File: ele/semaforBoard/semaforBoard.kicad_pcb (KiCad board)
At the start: 2 copper layers, 52.1 x 21.6 mm, 25 parts, among them J1 RESET, J2 Flash_connector, J3 USB_A, Q1 BC817, Q2 BC817, Q3 BC817, SW1 SW_Push, U1 ESP-01, U2 AMS1117-3.3

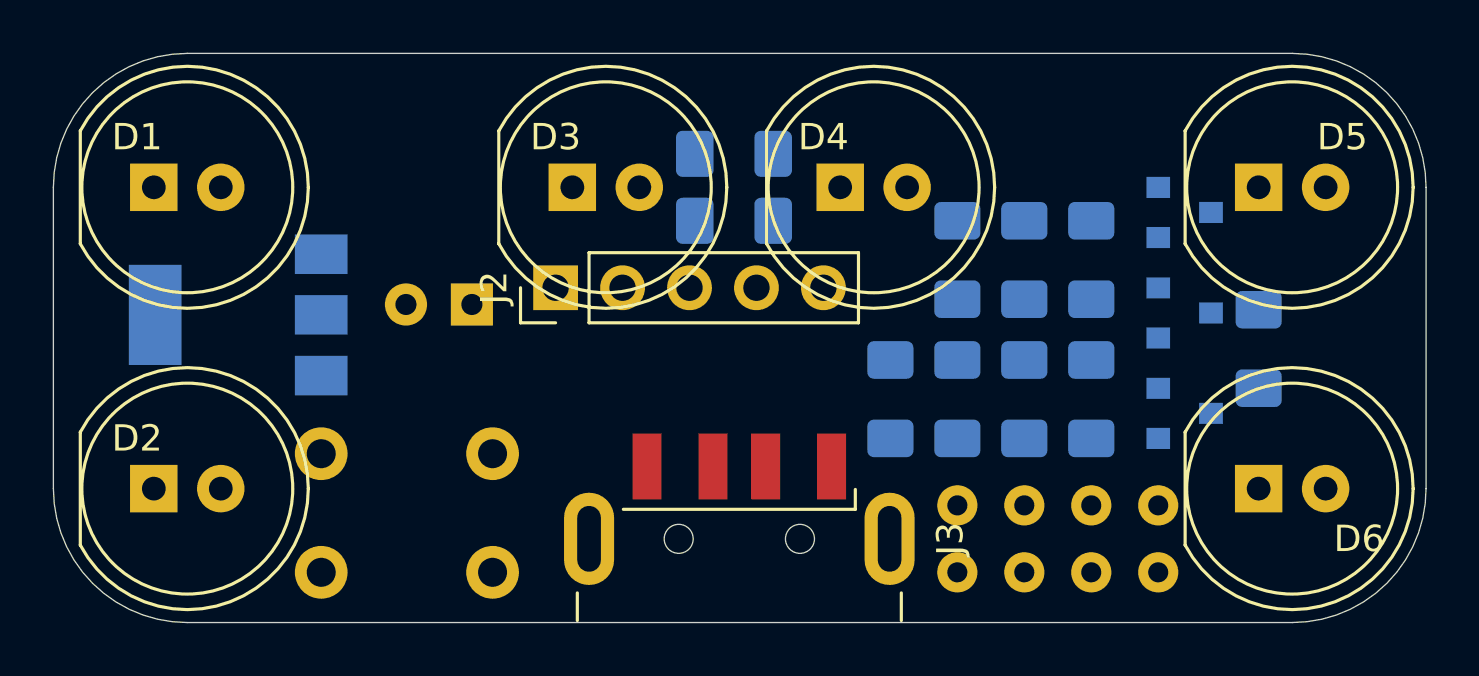
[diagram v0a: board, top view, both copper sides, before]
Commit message: Component placement, logos.
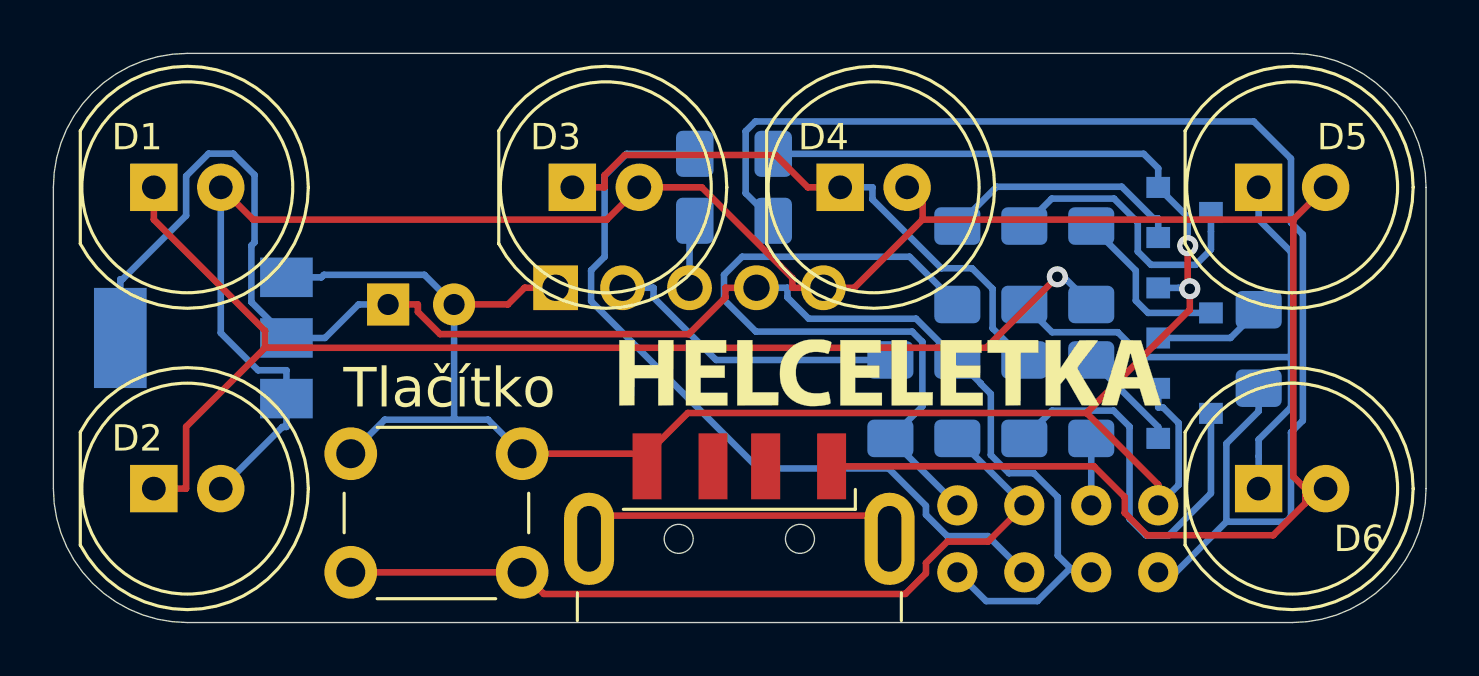
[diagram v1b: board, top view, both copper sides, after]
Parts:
- added G***: LOGO, semaforBoard:Robotarna, F.Cu at (154.4, 82.0)
- added G1: LOGO, semaforBoard:Robotarna, B.Cu at (129.0, 84.6)
- added G2: LOGO, semaforBoard:Helceletka, F.Cu at (148.6, 94.6)
- J2: moved to B.Cu
- SW1: moved to F.Cu
- moved SW1 4.64 mm to (134.6, 102.2)
- moved C1 3.18 mm to (129.5, 92.1), turned to 0 degrees
- moved U2 1.58 mm to (122.5, 93.3)
- moved R3 0.20 mm to (151.1, 90.6)
- moved R5 0.20 mm to (156.2, 90.6)
- moved R7 0.20 mm to (153.7, 90.6)
- turned J2 to 270 degrees
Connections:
- J2 pad 4: Net-(J2-Pad4) -> +3V3
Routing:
- net +5V: track 0.00 -> 93.6 mm
- net GND: track 0.00 -> 82.7 mm, vias 0 -> 2
- net +3V3: track 0.00 -> 62.7 mm
- net LED-A: track 0.00 -> 50.7 mm
- net Net-(D1-Pad1): track 0.00 -> 48.5 mm, vias 0 -> 1
- net BUTTON: track 0.00 -> 31.1 mm
- net RESET: track 0.00 -> 29.6 mm
- net LED-C: track 0.00 -> 26.8 mm
- net Net-(D5-Pad1): track 0.00 -> 23.4 mm
- net Net-(D3-Pad1): track 0.00 -> 22.3 mm
- net Net-(Q2-Pad3): track 0.00 -> 15.2 mm
- net Net-(J3-Pad5): track 0.00 -> 12.1 mm
- net Net-(J2-Pad2): track 0.00 -> 11.5 mm
- net Net-(Q3-Pad3): track 0.00 -> 10.8 mm
- net Net-(Q3-Pad1): track 0.00 -> 9.46 mm
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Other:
- board text added: "5V 3V3 TX RX GND"
- board text added: "Boot"
- board text added: "Semafor v0.1 05/20"
- board text added: "Tlačítko"

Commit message: Removed "tlačítko" marking, mount of button now possible on both-sides. Gen. gerbers.
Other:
- board text removed: "Tlačítko"

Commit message: Updated schmatic for CH340G.
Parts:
- removed J2: Flash_connector, semaforBoard:PinHeader_1x05_P2.54mm_Vertical
- added 100nF1: C, Capacitor_SMD:C_1206_3216Metric_Pad1.42x1.75mm_HandSolder, F.Cu at (107.7, 128.3)
- added 100nF2: C, Capacitor_SMD:C_1206_3216Metric_Pad1.42x1.75mm_HandSolder, F.Cu at (107.7, 133.1)
- added 22pF1: C, Capacitor_SMD:C_1206_3216Metric_Pad1.42x1.75mm_HandSolder, F.Cu at (113.6, 128.3)
- added 22pF2: C, Capacitor_SMD:C_1206_3216Metric_Pad1.42x1.75mm_HandSolder, F.Cu at (129.3, 121.6)
- added Q4: BC817, Package_TO_SOT_SMD:SOT-23, F.Cu at (128.5, 125.5)
- added Q5: BC817, Package_TO_SOT_SMD:SOT-23, F.Cu at (128.5, 130.1)
- added R10: 12k, Resistor_SMD:R_1206_3216Metric_Pad1.42x1.75mm_HandSolder, F.Cu at (113.6, 131.6)
- added U3: CH340G, Package_SO:SOIC-16_3.9x9.9mm_P1.27mm, F.Cu at (122.1, 125.7)
- added Y1: Crystal, Crystal:Crystal_HC49-4H_Vertical, F.Cu at (108.8, 123.3)
- J1: footprint Resistor_SMD:R_1206_3216Metric_Pad1.42x1.75mm_HandSolder -> Connector_PinHeader_2.54mm:PinHeader_1x02_P2.54mm_Vertical
- R4: value 22k -> 12k
- R8, R9: value 330R -> 1.2k
- moved R7 2.20 mm to (154.3, 88.5)
- moved R3 2.20 mm to (151.8, 88.5)
- moved R5 2.20 mm to (156.8, 88.5)
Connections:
- J3 pad 2: Net-(J3-Pad2) -> D-
- J3 pad 3: Net-(J3-Pad3) -> D+
- J3 pad 5: Net-(J3-Pad5) -> GND
- R8 pad 1: LED-C -> LED-A
- R9 pad 1: LED-A -> LED-C
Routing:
- net +5V: track 93.6 -> 0.00 mm
- net GND: track 82.7 -> 0.00 mm, vias 2 -> 0
- net +3V3: track 62.7 -> 0.00 mm
- net LED-A: track 50.7 -> 0.00 mm
- net Net-(D1-Pad1): track 48.5 -> 0.00 mm, vias 1 -> 0
- net BUTTON: track 31.1 -> 0.00 mm
- net RESET: track 29.6 -> 0.00 mm
- net LED-C: track 26.8 -> 0.00 mm
- net Net-(D5-Pad1): track 23.4 -> 0.00 mm
- net Net-(D3-Pad1): track 22.3 -> 0.00 mm
- net Net-(Q2-Pad3): track 15.2 -> 0.00 mm
- net Net-(J3-Pad5): track 12.1 -> 0.00 mm
- net Net-(R8-Pad2): track 11.5 -> 0.00 mm
- net Net-(Q3-Pad3): track 10.8 -> 0.00 mm
- net Net-(Q3-Pad1): track 9.46 -> 0.00 mm
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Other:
- board text removed: "5V 3V3 TX RX GND"

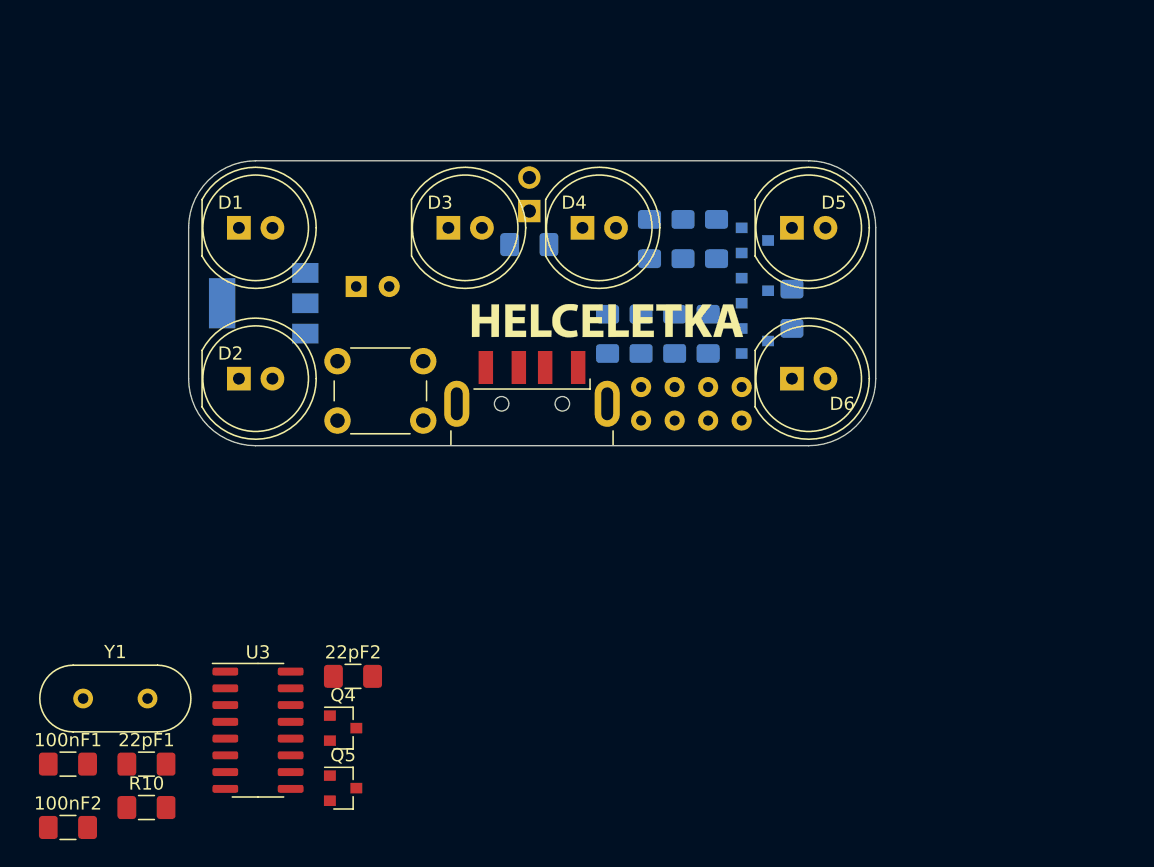
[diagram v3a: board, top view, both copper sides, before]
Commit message: 10mm leds. PCB routed.
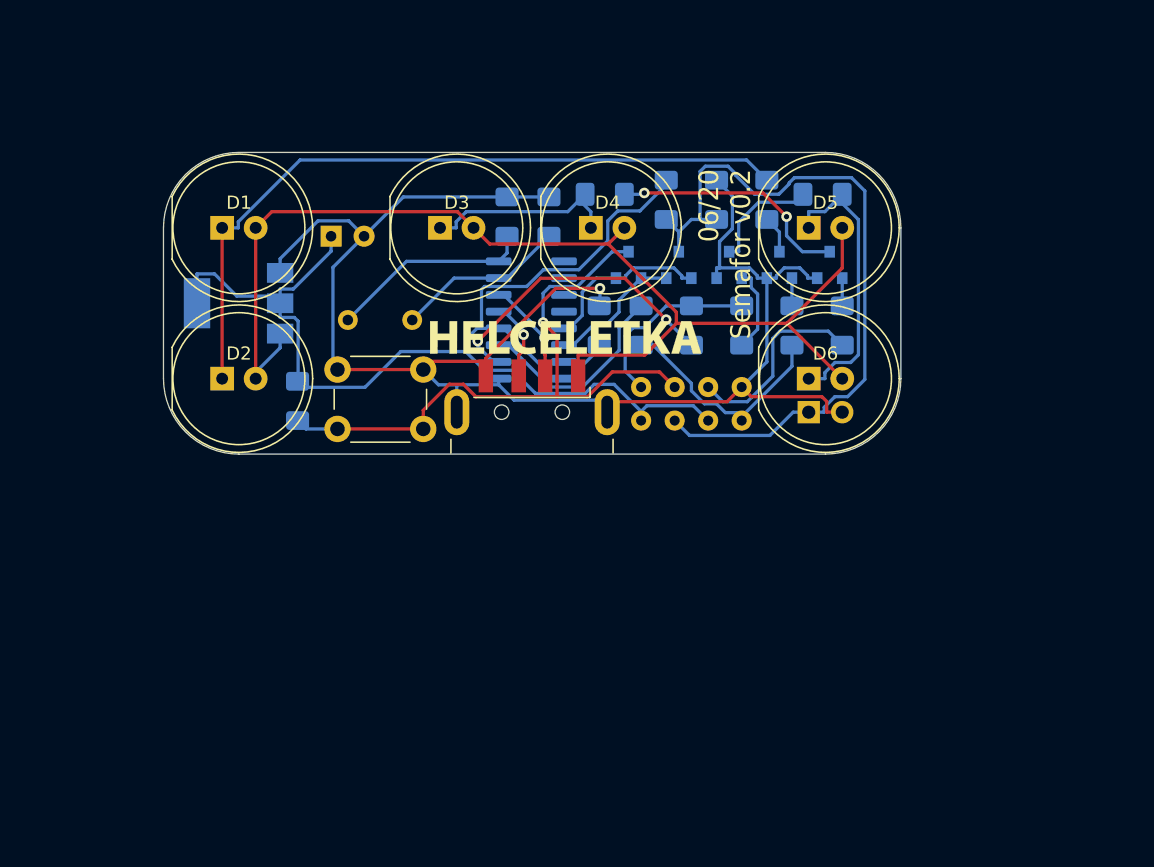
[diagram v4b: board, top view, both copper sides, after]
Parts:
- removed 100nF2, 22pF1, 22pF2: C, Capacitor_SMD:C_1206_3216Metric_Pad1.42x1.75mm_HandSolder
- added C3: 22pF, Capacitor_SMD:C_1206_3216Metric_Pad1.42x1.75mm_HandSolder, B.Cu at (144.1, 86.8)
- added C4: 100nF, Capacitor_SMD:C_1206_3216Metric_Pad1.42x1.75mm_HandSolder, B.Cu at (148.0, 95.0)
- added C5: 22pF, Capacitor_SMD:C_1206_3216Metric_Pad1.42x1.75mm_HandSolder, B.Cu at (141.0, 86.8)
- C2: renamed from 100nF1; value C -> 100nF; moved to B.Cu
- D1, D2, D3, D4, D5, D6: footprint LED_THT:LED_D8.0mm -> LED_THT:LED_D10.0mm
- J1: footprint Connector_PinHeader_2.54mm:PinHeader_1x02_P2.54mm_Vertical -> semaforBoard:PinHeader_1x02_P2.54mm_Vertical
- Q4, Q5, R10, U3, Y1: moved to B.Cu
- moved C2 65.1 mm to (156.8, 85.5), turned to 90 degrees
- moved R10 60.6 mm to (153.0, 85.5), turned to 90 degrees
- moved Q5 45.2 mm to (150.2, 90.4), turned to 90 degrees
- moved Q4 43.3 mm to (154.0, 90.4), turned to 90 degrees
- moved Y1 38.0 mm to (133.8, 94.6), turned to 180 degrees
- moved U3 37.4 mm to (142.8, 94.6)
- moved R4 26.5 mm to (125.1, 100.7)
- moved J1 26.1 mm to (163.8, 101.6), turned to 270 degrees
- moved R9 13.7 mm to (154.9, 95.0), turned to 270 degrees
- moved R6 11.8 mm to (148.4, 85.1), turned to 0 degrees
- moved R7 11.1 mm to (164.9, 85.1), turned to 180 degrees
- moved R2 10.2 mm to (166.4, 95.0)
- moved R3 9.58 mm to (158.8, 95.0), turned to 90 degrees
- moved Q2 8.09 mm to (165.4, 90.4), turned to 90 degrees
- moved R5 4.83 mm to (160.7, 85.5), turned to 270 degrees
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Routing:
- net GND: track 0.00 -> 124.5 mm, vias 0 -> 1
- net +3V3: track 0.00 -> 95.4 mm
- net +5V: track 0.00 -> 87.0 mm
- net Net-(D1-Pad1): track 0.00 -> 55.7 mm
- net RESET: track 0.00 -> 55.4 mm
- net BUTTON: track 0.00 -> 48.8 mm, vias 0 -> 1
- net Net-(R9-Pad2): track 0.00 -> 22.7 mm, vias 0 -> 2
- net Net-(D5-Pad1): track 0.00 -> 21.6 mm
- net Net-(Q2-Pad3): track 0.00 -> 18.3 mm, vias 0 -> 2
- net LED-A: track 0.00 -> 17.5 mm
- net Net-(R8-Pad2): track 0.00 -> 15.7 mm
- net Net-(C5-Pad1): track 0.00 -> 15.4 mm
- net LED-B: track 0.00 -> 14.9 mm
- net Net-(D3-Pad1): track 0.00 -> 14.8 mm
- net LED-C: track 0.00 -> 14.2 mm
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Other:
- board size 52.1 x 21.6 mm -> 55.9 x 22.9 mm
- board text added: "06/20 Semafor v0.2"
- board text added: "reset"
- board text removed: "Boot"
- board text removed: "Semafor v0.1 05/20"

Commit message: Panelized using kikit and generated fabrication data.
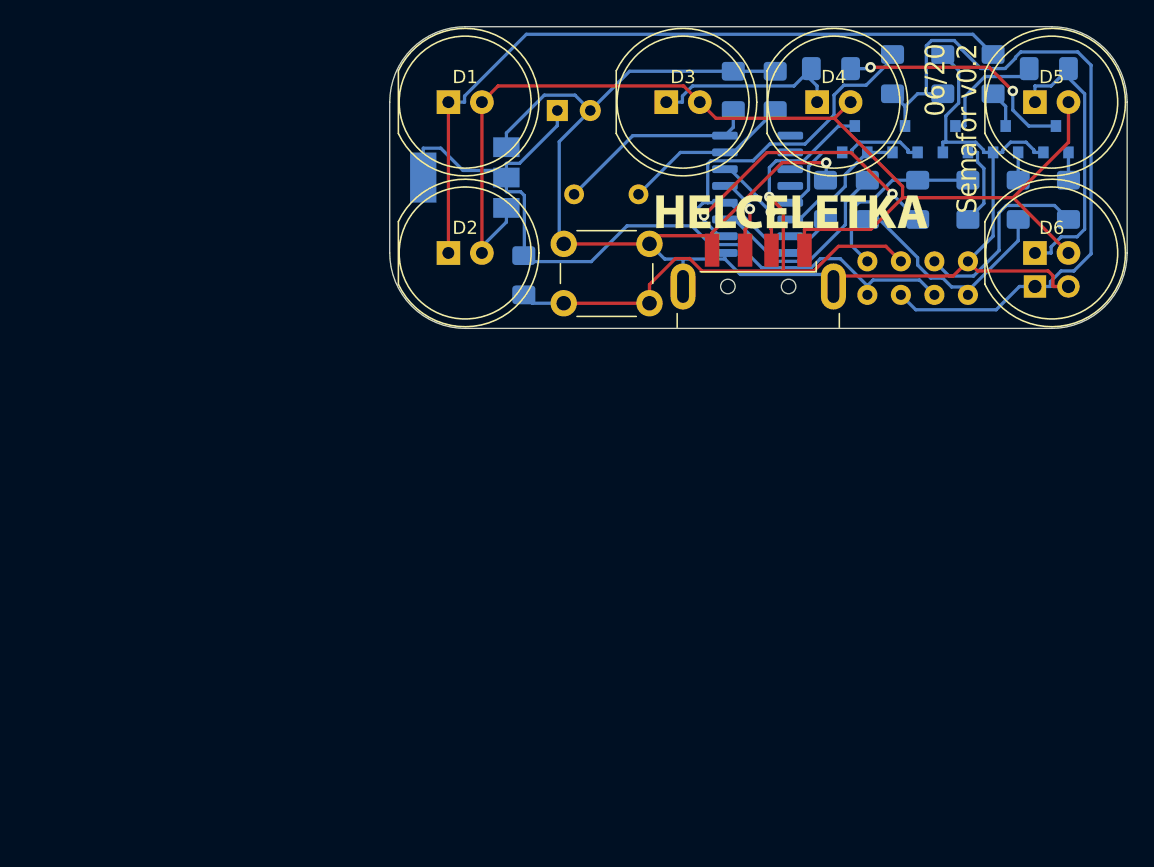
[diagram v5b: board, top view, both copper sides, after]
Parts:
- R1, R2, R3: value 22k -> 10k
- R10, R4: value 12k -> 10k
- R5, R6, R7: value 68R -> 75R
- R8, R9: value 1.2k -> 1k
- moved C5 19.6 mm to (158.1, 77.3)
- moved D2 19.6 mm to (136.5, 89.5)
- moved G2 19.6 mm to (162.6, 86.4)
- moved R1 19.6 mm to (179.7, 85.5)
- moved R3 19.6 mm to (175.9, 85.5)
- moved R4 19.6 mm to (142.2, 91.2)
- moved R8 19.6 mm to (168.3, 85.5)
- moved R9 19.6 mm to (172.1, 85.5)
- moved U2 19.6 mm to (137.8, 83.8)
- moved C2 19.6 mm to (174.0, 76.0)
- moved D1 19.6 mm to (136.5, 78.1)
- moved D3 19.6 mm to (153.0, 78.1)
- moved D4 19.6 mm to (164.5, 78.1)
- moved Q2 19.6 mm to (182.6, 80.9)
- moved R10 19.6 mm to (170.2, 76.0)
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
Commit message: Changed R2 LED-B-GPIO2 resistor from 10k to 33k for correct boot in KiCad project and excel production files. Added semafor riddle mode.
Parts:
- R2: value 10k -> 33k
